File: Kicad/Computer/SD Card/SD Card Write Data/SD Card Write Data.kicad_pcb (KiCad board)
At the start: 2 copper layers, 18.8 x 33.2 mm, 7 parts, among them IC1 AP7365-33WG-7, IC3 74LVC16373ADL,118, J1 Conn_02x12_Counter_Clockwise

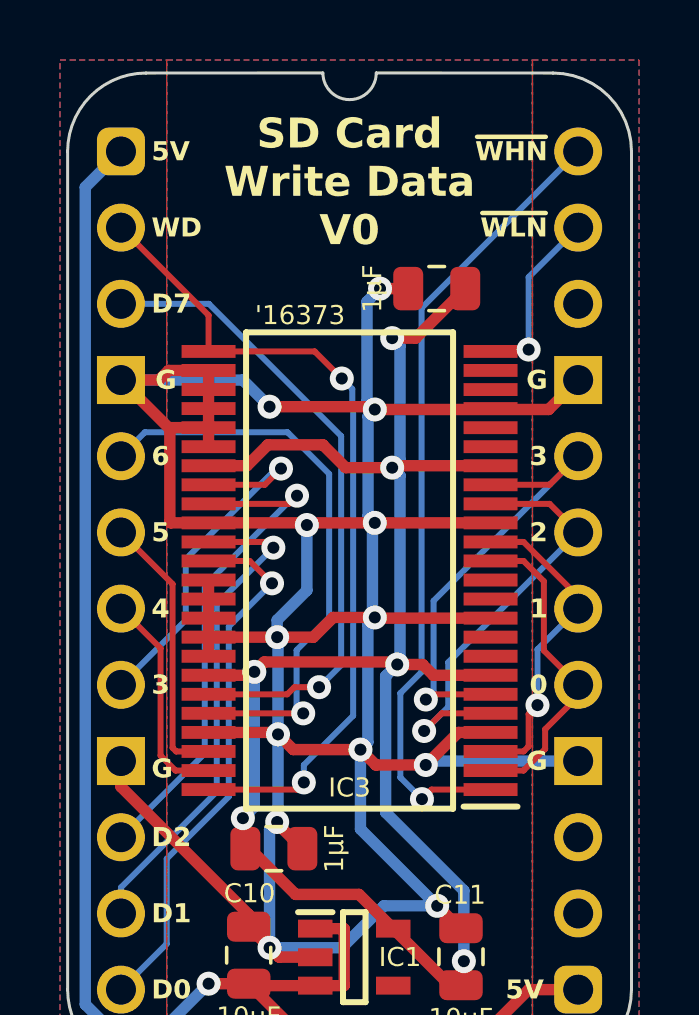
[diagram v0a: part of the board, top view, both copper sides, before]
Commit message: Generated Gerbers for SD Card components.
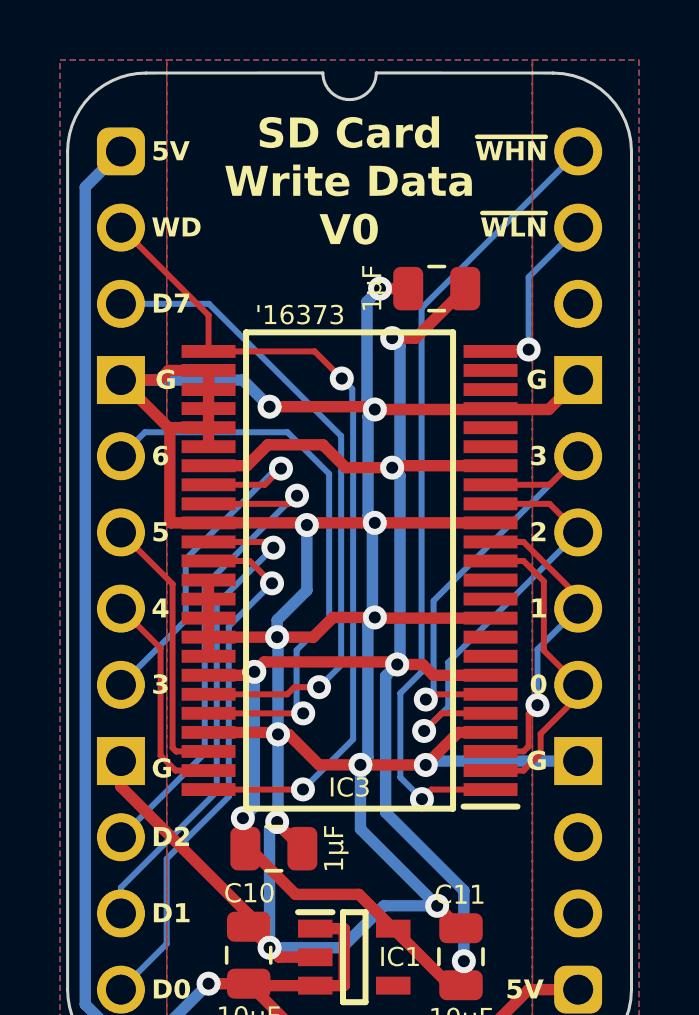
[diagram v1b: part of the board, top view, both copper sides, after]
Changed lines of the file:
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@@
 			(drillshape 0)
 			(scaleselection 1)
-			(outputdirectory "SD Card Write Data")
+			(outputdirectory "SD Card Read Data")
 		)
 	)
@@
 		(fp_arc
 			(start 14.404267 -2.613733)
-			(mid 16.252451 -1.848184)
+			(mid 16.252448 -1.848183)
 			(end 17.017999 -0.000001)
 			(stroke
@@
 	)
 	(segment
-		(start 97.395959 78.871383)
-		(end 99.06 78.871383)
-		(width 0.38)
-		(layer "F.Cu")
-		(net 9)
-	)
-	(segment
 		(start 94.107 80.822)
 		(end 94.107 80.772)
@@
 	)
 	(segment
+		(start 96.887971 78.871383)
+		(end 96.883588 78.867)
+		(width 0.38)
+		(layer "F.Cu")
+		(net 9)
+	)
+	(segment
 		(start 94.071 77.786766)
 		(end 91.820001 77.786766)
@@
 	)
 	(segment
-		(start 94.135 77.850766)
-		(end 94.643246 78.359012)
+		(start 94.487766 77.850766)
+		(end 95.504 78.867)
 		(width 0.38)
 		(layer "F.Cu")
@@
 	)
 	(segment
-		(start 96.883588 78.359012)
-		(end 97.395959 78.871383)
-		(width 0.38)
-		(layer "F.Cu")
-		(net 9)
-	)
-	(segment
 		(start 94.135 77.850766)
 		(end 94.071 77.786766)
@@
 	)
 	(segment
-		(start 94.643246 78.359012)
-		(end 96.883588 78.359012)
-		(width 0.38)
-		(layer "F.Cu")
-		(net 9)
-	)
-	(segment
 		(start 97.536 62.992)
 		(end 98.475 62.992)
@@
 	)
 	(segment
+		(start 99.06 78.871383)
+		(end 96.887971 78.871383)
+		(width 0.38)
+		(layer "F.Cu")
+		(net 9)
+	)
+	(segment
 		(start 91.82 72.706766)
 		(end 91.82 73.340766)
@@
 	)
 	(segment
+		(start 94.135 77.850766)
+		(end 94.487766 77.850766)
+		(width 0.38)
+		(layer "F.Cu")
+		(net 9)
+	)
+	(segment
+		(start 95.504 78.867)
+		(end 96.883588 78.867)
+		(width 0.38)
+		(layer "F.Cu")
+		(net 9)
+	)
+	(segment
 		(start 101.219999 73.976766)
 		(end 97.384042 73.976766)
@@
 	)
 	(via
-		(at 96.883588 78.359012)
+		(at 96.883588 78.867)
 		(size 0.8)
 		(drill 0.4)
@@
 	)
 	(segment
-		(start 97.130346 78.112254)
-		(end 96.883588 78.359012)
-		(width 0.38)
-		(layer "B.Cu")
-		(net 9)
-	)
-	(segment
 		(start 96.266 84.963)
 		(end 97.663 83.566)
@@
 	)
 	(segment
-		(start 97.361 73.953724)
-		(end 97.130346 74.184378)
-		(width 0.38)
-		(layer "B.Cu")
-		(net 9)
-	)
-	(segment
-		(start 96.883588 81.008588)
-		(end 96.883588 78.359012)
-		(width 0.38)
-		(layer "B.Cu")
-		(net 9)
-	)
-	(segment
 		(start 104.14 78.74)
 		(end 99.191383 78.74)
@@
 	)
 	(segment
-		(start 97.130346 74.184378)
-		(end 97.130346 78.112254)
-		(width 0.38)
-		(layer "B.Cu")
-		(net 9)
-	)
-	(segment
 		(start 97.663 83.566)
 		(end 99.441 83.566)
@@
 	)
 	(segment
+		(start 97.130346 78.620242)
+		(end 96.883588 78.867)
+		(width 0.38)
+		(layer "B.Cu")
+		(net 9)
+	)
+	(segment
 		(start 93.853 84.963)
 		(end 93.853 81.026)
@@
 	)
 	(segment
-		(start 99.441 83.566)
-		(end 96.883588 81.008588)
+		(start 96.883588 81.008588)
+		(end 96.883588 78.867)
+		(width 0.38)
+		(layer "B.Cu")
+		(net 9)
+	)
+	(segment
+		(start 97.130346 74.184378)
+		(end 97.130346 78.620242)
 		(width 0.38)
 		(layer "B.Cu")
@@
 	)
 	(segment
+		(start 99.441 83.566)
+		(end 96.883588 81.008588)
+		(width 0.38)
+		(layer "B.Cu")
+		(net 9)
+	)
+	(segment
+		(start 97.361 73.953724)
+		(end 97.130346 74.184378)
+		(width 0.38)
+		(layer "B.Cu")
+		(net 9)
+	)
+	(segment
 		(start 97.282 70.879766)
 		(end 97.282 73.874724)
@@
 	)
 	(segment
-		(start 91.82 79.690766)
-		(end 94.758234 79.690766)
+		(start 91.82 65.086766)
+		(end 95.358518 65.086766)
 		(width 0.2)
 		(layer "F.Cu")
@@
 	)
 	(segment
-		(start 91.82 65.086766)
-		(end 95.358518 65.086766)
+		(start 95.358518 65.086766)
+		(end 96.261 65.989248)
 		(width 0.2)
 		(layer "F.Cu")
@@
 	)
 	(segment
-		(start 94.758234 79.690766)
-		(end 94.996 79.453)
+		(start 94.962645 79.690766)
+		(end 94.966888 79.686523)
 		(width 0.2)
 		(layer "F.Cu")
@@
 	)
 	(segment
-		(start 95.358518 65.086766)
-		(end 96.261 65.989248)
+		(start 91.82 63.88)
+		(end 91.82 65.086766)
 		(width 0.2)
 		(layer "F.Cu")
@@
 	)
 	(segment
-		(start 91.82 63.88)
-		(end 91.82 65.086766)
+		(start 91.82 79.690766)
+		(end 94.962645 79.690766)
 		(width 0.2)
 		(layer "F.Cu")
@@
 	)
 	(via
-		(at 94.996 79.453)
+		(at 94.966888 79.686523)
 		(size 0.8)
 		(drill 0.4)
@@
 	)
 	(segment
-		(start 96.640339 66.99407)
+		(start 96.611 66.339248)
 		(end 96.611 66.964731)
 		(width 0.2)
@@
 	)
 	(segment
-		(start 94.996 78.872339)
-		(end 96.640339 77.228)
+		(start 96.261 65.989248)
+		(end 96.611 66.339248)
 		(width 0.2)
 		(layer "B.Cu")
@@
 	)
 	(segment
-		(start 96.640339 77.228)
-		(end 96.640339 66.99407)
+		(start 96.640339 66.99407)
+		(end 96.640339 78.013072)
 		(width 0.2)
 		(layer "B.Cu")
@@
 	(segment
 		(start 96.611 66.964731)
-		(end 96.611 66.339248)
-		(width 0.2)
-		(layer "B.Cu")
-		(net 16)
-	)
-	(segment
-		(start 94.996 79.453)
-		(end 94.996 78.872339)
+		(end 96.640339 66.99407)
 		(width 0.2)
 		(layer "B.Cu")
@@
 	)
 	(segment
-		(start 96.611 66.339248)
-		(end 96.261 65.989248)
+		(start 96.640339 78.013072)
+		(end 94.966888 79.686523)
 		(width 0.2)
 		(layer "B.Cu")
@@
 	)
 	(segment
-		(start 102.997 75.057)
-		(end 104.14 76.2)
+		(start 102.889 78.487766)
+		(end 102.889 77.832)
 		(width 0.2)
 		(layer "F.Cu")
@@
 	)
 	(segment
-		(start 103.04 77.681)
-		(end 104.14 76.581)
+		(start 102.32 79.056766)
+		(end 102.889 78.487766)
 		(width 0.2)
 		(layer "F.Cu")
@@
 	)
 	(segment
-		(start 101.22 72.070766)
-		(end 102.32 72.070766)
+		(start 102.997 75.057)
+		(end 104.14 76.2)
 		(width 0.2)
 		(layer "F.Cu")
@@
 	)
 	(segment
-		(start 102.32 72.070766)
-		(end 102.997 72.747766)
+		(start 101.22 72.070766)
+		(end 102.32 72.070766)
 		(width 0.2)
 		(layer "F.Cu")
@@
 	)
 	(segment
-		(start 103.04 78.336766)
-		(end 103.04 77.681)
+		(start 102.889 77.832)
+		(end 104.14 76.581)
 		(width 0.2)
 		(layer "F.Cu")
@@
 	)
 	(segment
-		(start 101.22 79.056766)
-		(end 102.32 79.056766)
+		(start 102.32 72.070766)
+		(end 102.997 72.747766)
 		(width 0.2)
 		(layer "F.Cu")
@@
 	)
 	(segment
-		(start 102.32 79.056766)
-		(end 103.04 78.336766)
+		(start 101.22 79.056766)
+		(end 102.32 79.056766)
 		(width 0.2)
 		(layer "F.Cu")

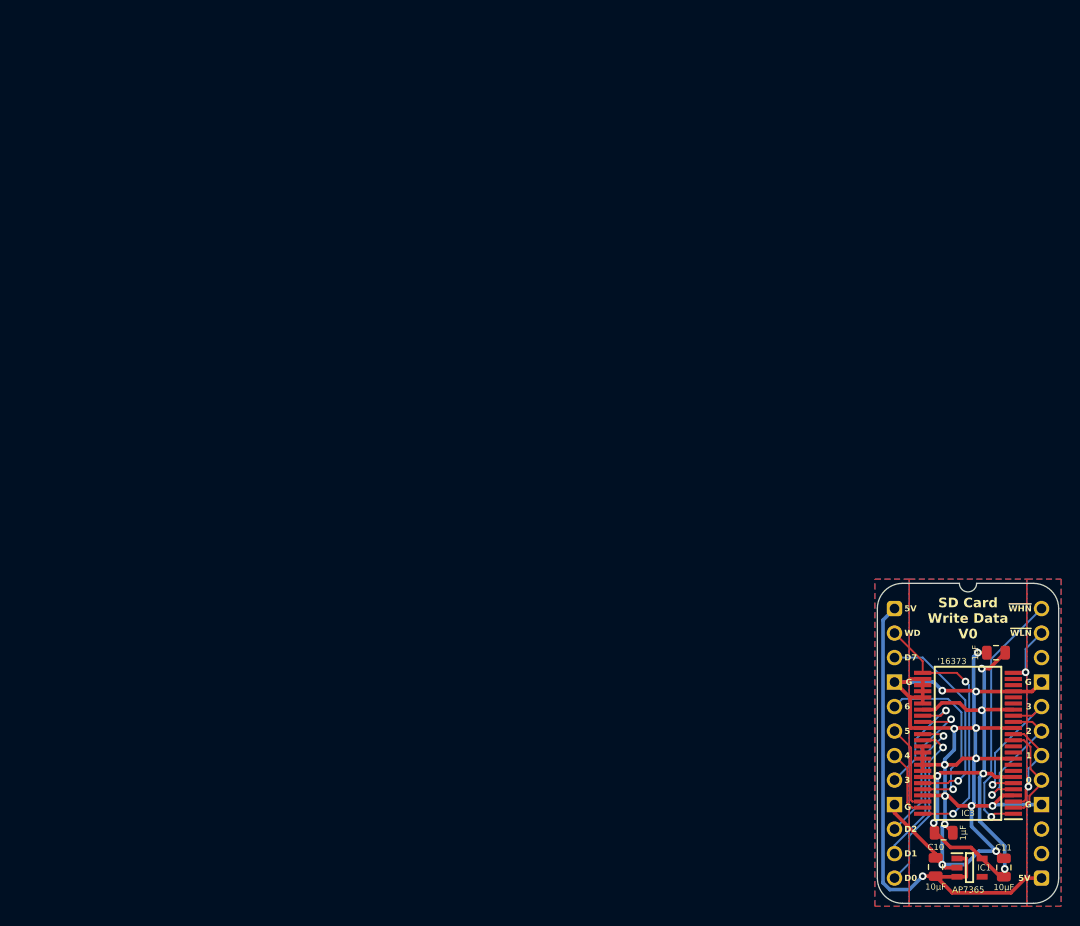
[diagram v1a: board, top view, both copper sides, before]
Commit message: Use VRML instead of STEPs for SD Card Board models.
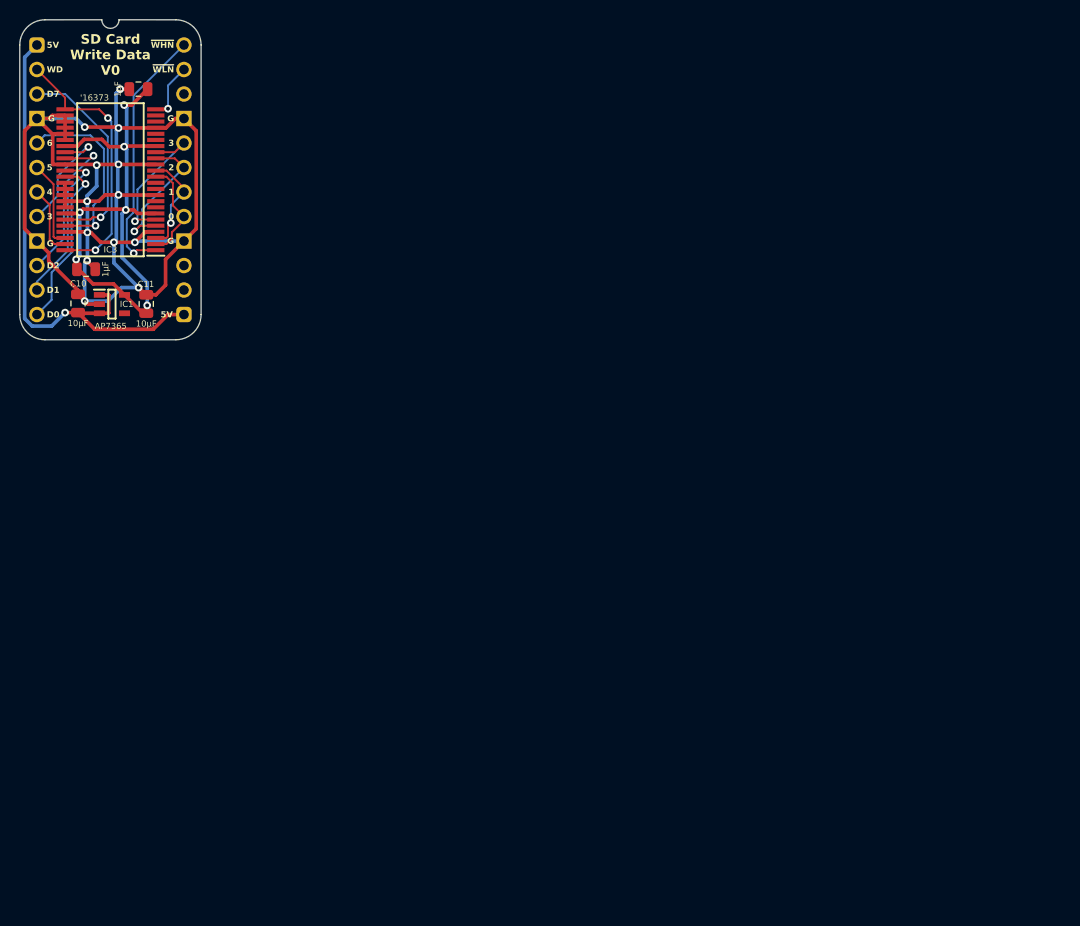
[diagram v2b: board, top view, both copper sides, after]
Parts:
- added J2: Pin_Header_01x12, SamacSys_Parts:PinHeader_1x12_P2.54mm_Vertical, B.Cu at (0.00, 0.00)
- added J3: Pin_Header_01x12, SamacSys_Parts:PinHeader_1x12_P2.54mm_Vertical, B.Cu at (15.2, 0.00)
- moved C1 106.4 mm to (5.08, 23.2)
- moved C10 106.4 mm to (4.26, 26.8)
- moved C11 106.4 mm to (11.3, 26.9)
- moved C4 106.4 mm to (10.5, 4.57)
- moved IC1 106.4 mm to (7.78, 26.9)
- moved J1 106.4 mm to (0.00, 0.00)
- moved IC3 106.4 mm to (7.62, 14.0)
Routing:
- net GND: track 123.0 -> 158.3 mm
- removed copper zone on B.Cu, net GND
- removed copper zone on F.Cu, net GND

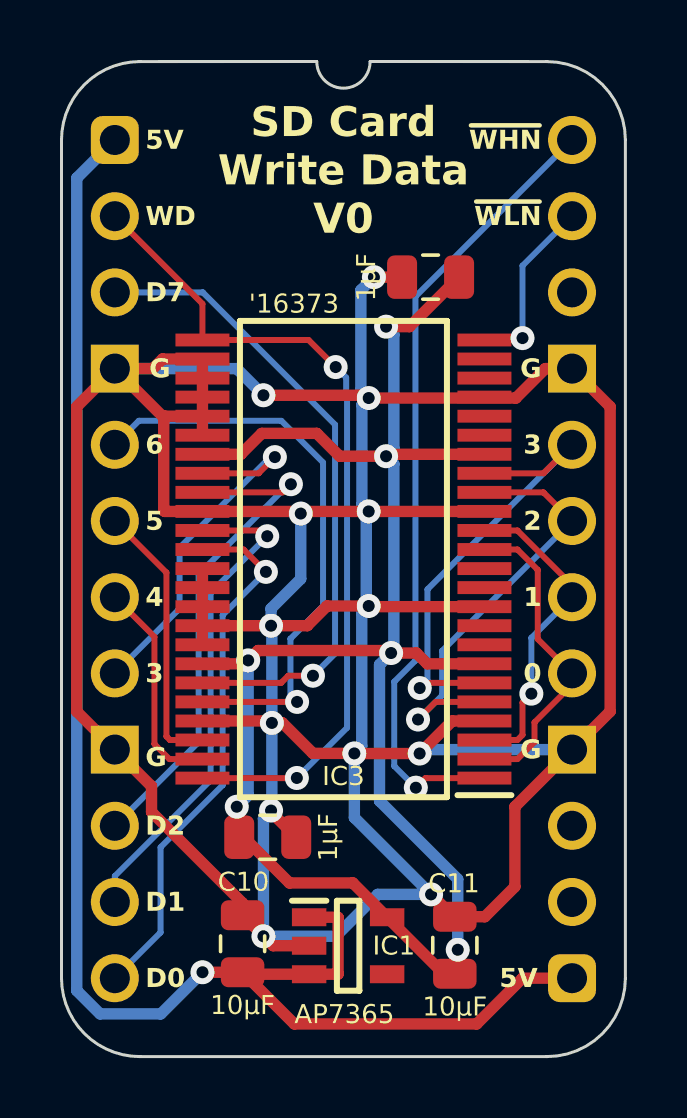
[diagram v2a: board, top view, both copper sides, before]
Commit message: Rounded SD Card Write traces.
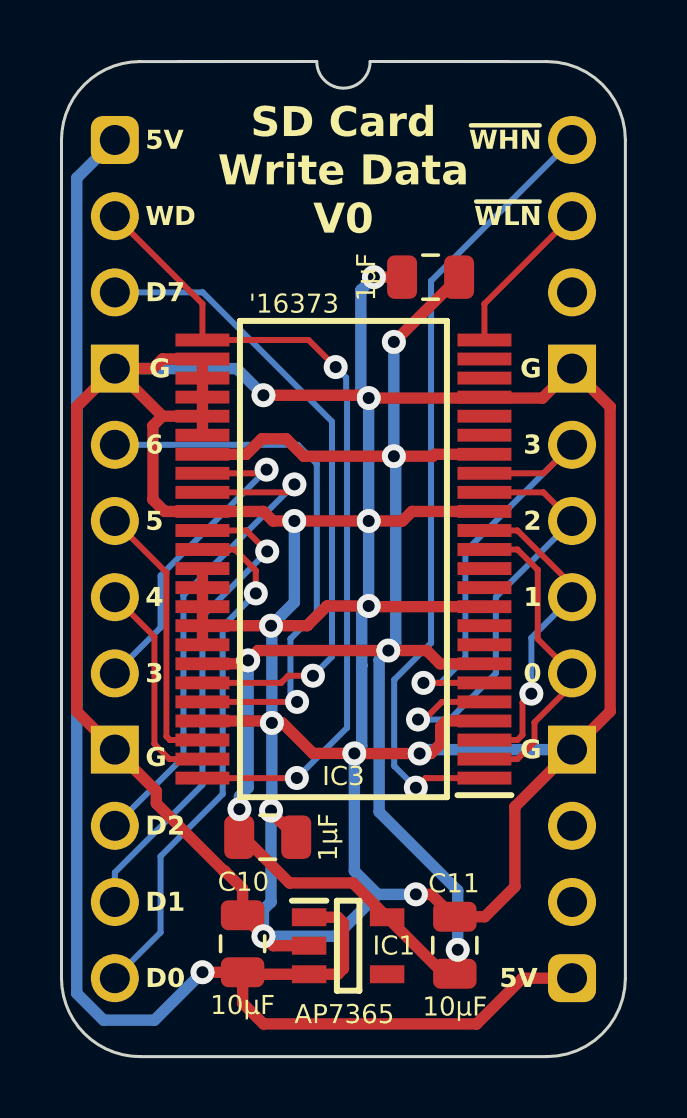
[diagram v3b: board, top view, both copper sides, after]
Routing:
- net D3: track 12.1 -> 11.1 mm
- net /3.3V: track 60.8 -> 59.7 mm
- net D6: track 19.5 -> 18.5 mm
- net 5V: track 53.6 -> 54.6 mm
- net ~{Write Low Nybble}: track 6.04 -> 5.34 mm, vias 1 -> 0
- net DAT2: track 14.5 -> 15.1 mm

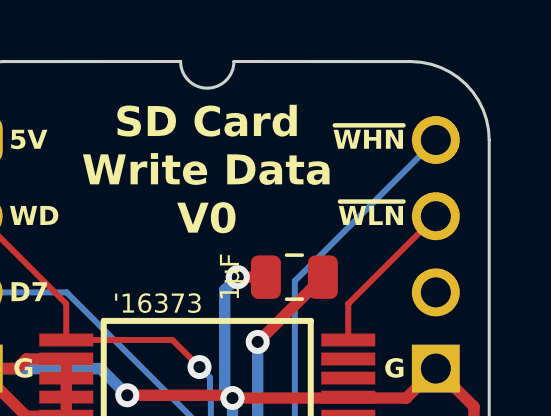
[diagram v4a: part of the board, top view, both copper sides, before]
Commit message: PS2 and SD Card boards with proper board schematic symbol and global labels.
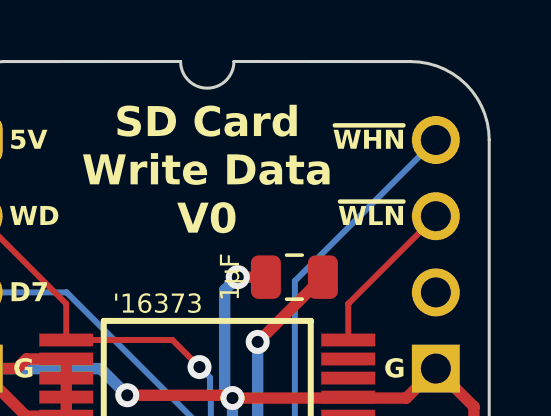
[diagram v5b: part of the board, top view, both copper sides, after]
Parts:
- removed J2, J3: Pin_Header_01x12, SamacSys_Parts:PinHeader_1x12_P2.54mm_Vertical
- J1: value Conn_02x12_Counter_Clockwise -> Board 2x12 W15.24mm
